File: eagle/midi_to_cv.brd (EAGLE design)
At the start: 100.1 x 82 mm, 35 parts, among them IC2 4504N, IC3 4099N, U1 ATMEGA328P_PDIP

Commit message: starting brd and dac library
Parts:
- removed D1: 1N4148DO35-10, diode:DO35-10
- removed OK1: 6N138, optocoupler:DIL08
- removed PAD1: midi pin 4, wirepad:2,54/0,9
- removed PAD2: midi pin 5, wirepad:2,54/0,9
- removed R2: 220, rcl:0207/10
- removed R3: 270, rcl:0207/10
- added D2: (no value), SparkFun-DiscreteSemi:DIODE-1N4148
- added MIDI_IN: 22-23-2021, con-molex:22-23-2021
- added OK2: 6N138, optocoupler:DIL08
- added R5: 220, rcl:0207/10
- added R6: 270, rcl:0207/10
- added U$11: TLV5628C/I, Texas Instruments_By_element14_Batch_1:DIP16
- moved U$10 300.9 mm to (-69.8, 57.1)
- moved U$9 288.2 mm to (-48.3, 57.1)
- moved U$8 277.1 mm to (-26.7, 57.1)
- moved U$7 256.2 mm to (-69.8, 45.7)
- moved U$6 243.3 mm to (-48.3, 45.7)
- moved R15 228.2 mm to (-57.1, 82.5)
- moved U$2 222.7 mm to (-69.8, 34.3)
- moved U$1 209.5 mm to (-48.3, 34.3)
- moved U$4 204.0 mm to (20.3, 61.0), turned to 270 degrees
- moved C6 203.3 mm to (16.5, 55.9), turned to 180 degrees
- moved C7 199.4 mm to (8.89, 55.9), turned to 180 degrees
- moved U$5 197.9 mm to (5.08, 61.0), turned to 270 degrees
- moved C4 197.1 mm to (16.5, 61.0), turned to 180 degrees
- moved PWR1 195.4 mm to (14.0, 72.4)
- moved C5 192.9 mm to (10.2, 61.0), turned to 180 degrees
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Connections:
- new net N$17: D2.A, MIDI_IN.2, OK2.3
- new net N$18: D2.C, OK2.2, R5.2
- new net N$19: MIDI_IN.1, R5.1
- new net N$20: OK2.6, R6.1
- new net N$21: U$11.15, U$7.13, U$7.14
- new net N$22: U$11.7, U$8.13, U$8.14
- new net N$24: U$11.8, U$9.13, U$9.14
- new net N$28: U$10.13, U$10.14, U$11.9
- new net N$29: U$1.13, U$1.14, U$11.10
- net +12V: now also U$10.10, U$10.9, U$6.10, U$6.9
- net +5V: now also IC3.2, OK2.8, R6.2, U$11.11, U$11.14, U$11.6; no longer OK1.8, R3.2
- net GND: now also OK2.5, U$11.13, U$11.3; no longer OK1.5
- net N$14: now also U$11.5
- net N$15: now also U$11.12
- net N$23: now also U1.4; no longer U1.6
- net N$25: now also U1.6; no longer U1.4
- net N$27: now also U$11.4
- net N$3: now also U$11.2, U$3.13, U$3.14; no longer D1.A, OK1.3, PAD2.1
- net N$30: no longer OK1.6, R3.1
- net N$7: now also U$11.1, U$2.13, U$2.14; no longer D1.C, OK1.2, R2.2
- net N$8: now also U$11.16, U$6.13, U$6.14; no longer PAD1.1, R2.1
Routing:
- net +5V: track 128.9 -> 0.00 mm, vias 2 -> 0
- net GND: track 126.0 -> 0.00 mm
- net N$30: track 31.5 -> 0.00 mm
- net N$1: track 23.0 -> 0.00 mm
- net N$7: track 13.3 -> 0.00 mm
- net N$27: track 12.8 -> 0.00 mm
- net N$4: track 11.7 -> 0.00 mm
- net N$5: track 10.7 -> 0.00 mm
- net N$10: track 10.6 -> 0.00 mm
- net N$3: track 10.5 -> 0.00 mm
- net N$14: track 10.3 -> 0.00 mm
- net N$15: track 8.15 -> 0.00 mm
- net N$8: track 6.13 -> 0.00 mm
- net N$11: track 2.09 -> 0.00 mm
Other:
- board size 100.1 x 82 mm -> 100 x 80 mm

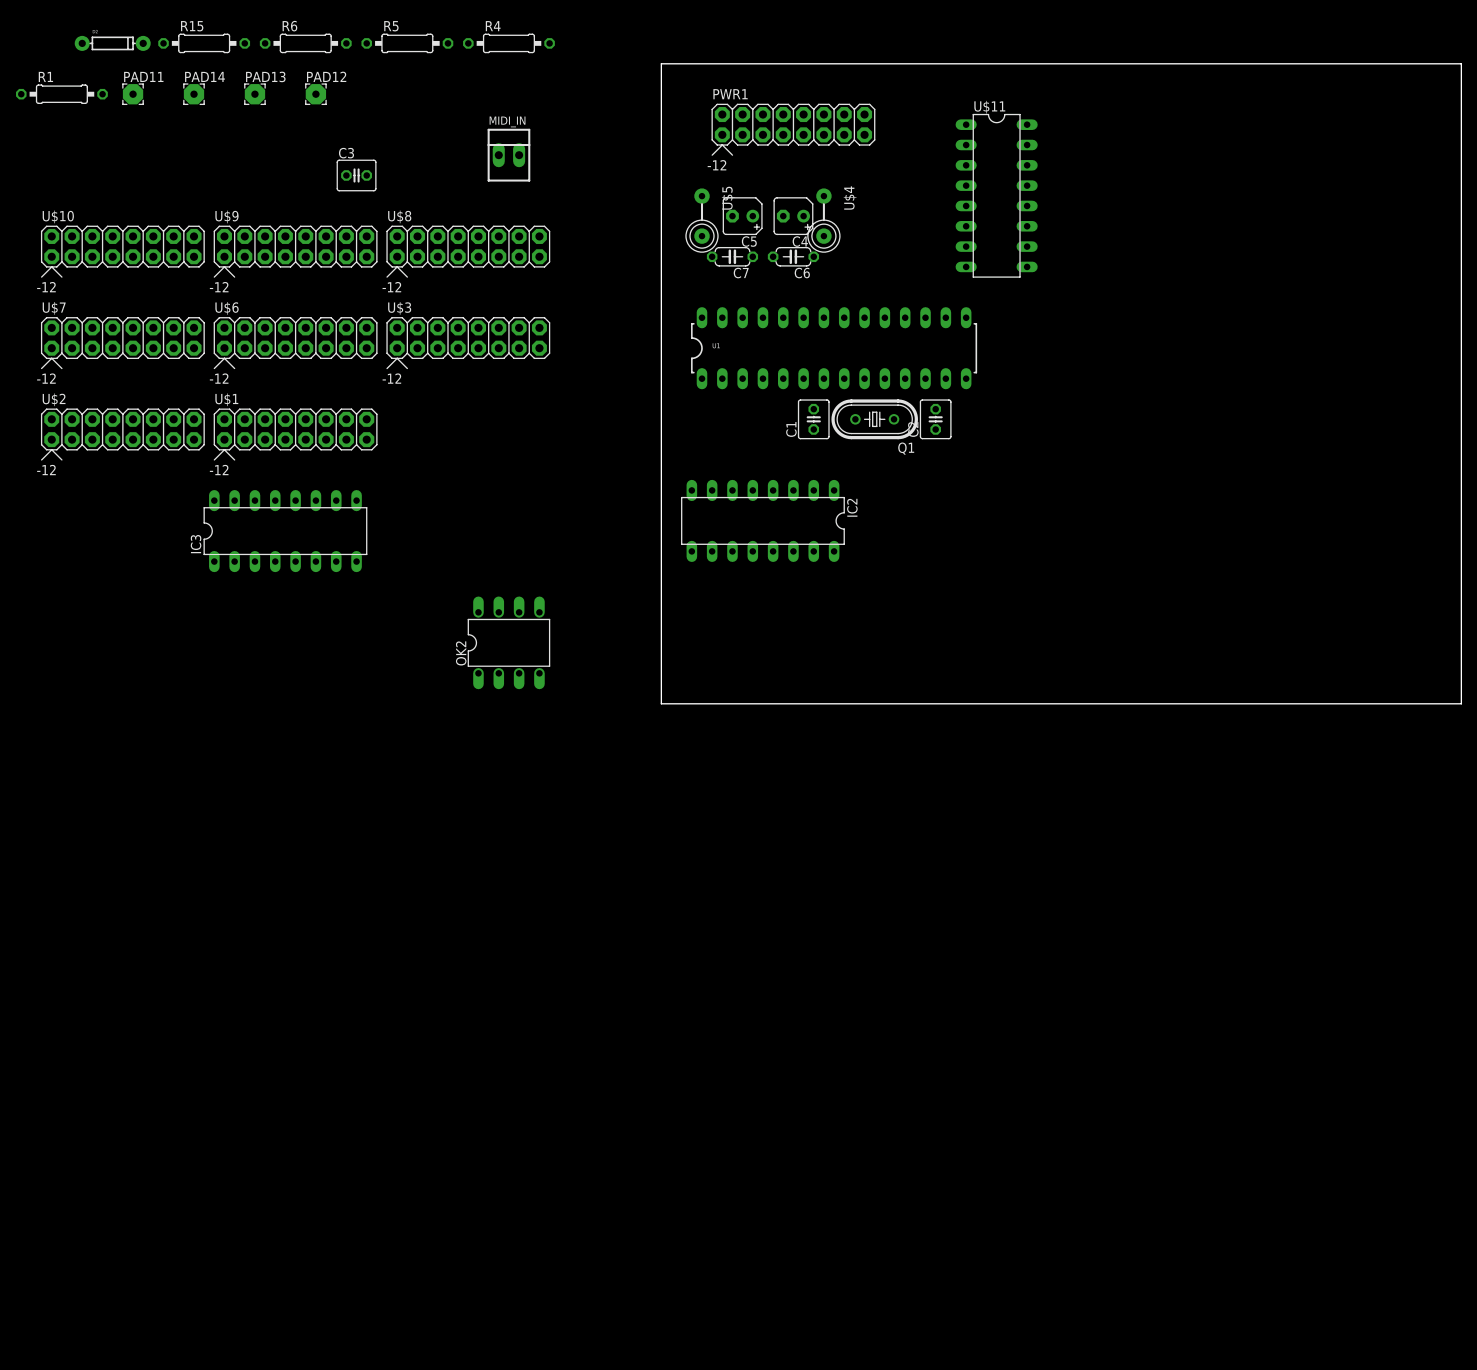
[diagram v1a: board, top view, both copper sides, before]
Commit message: adding output resistors
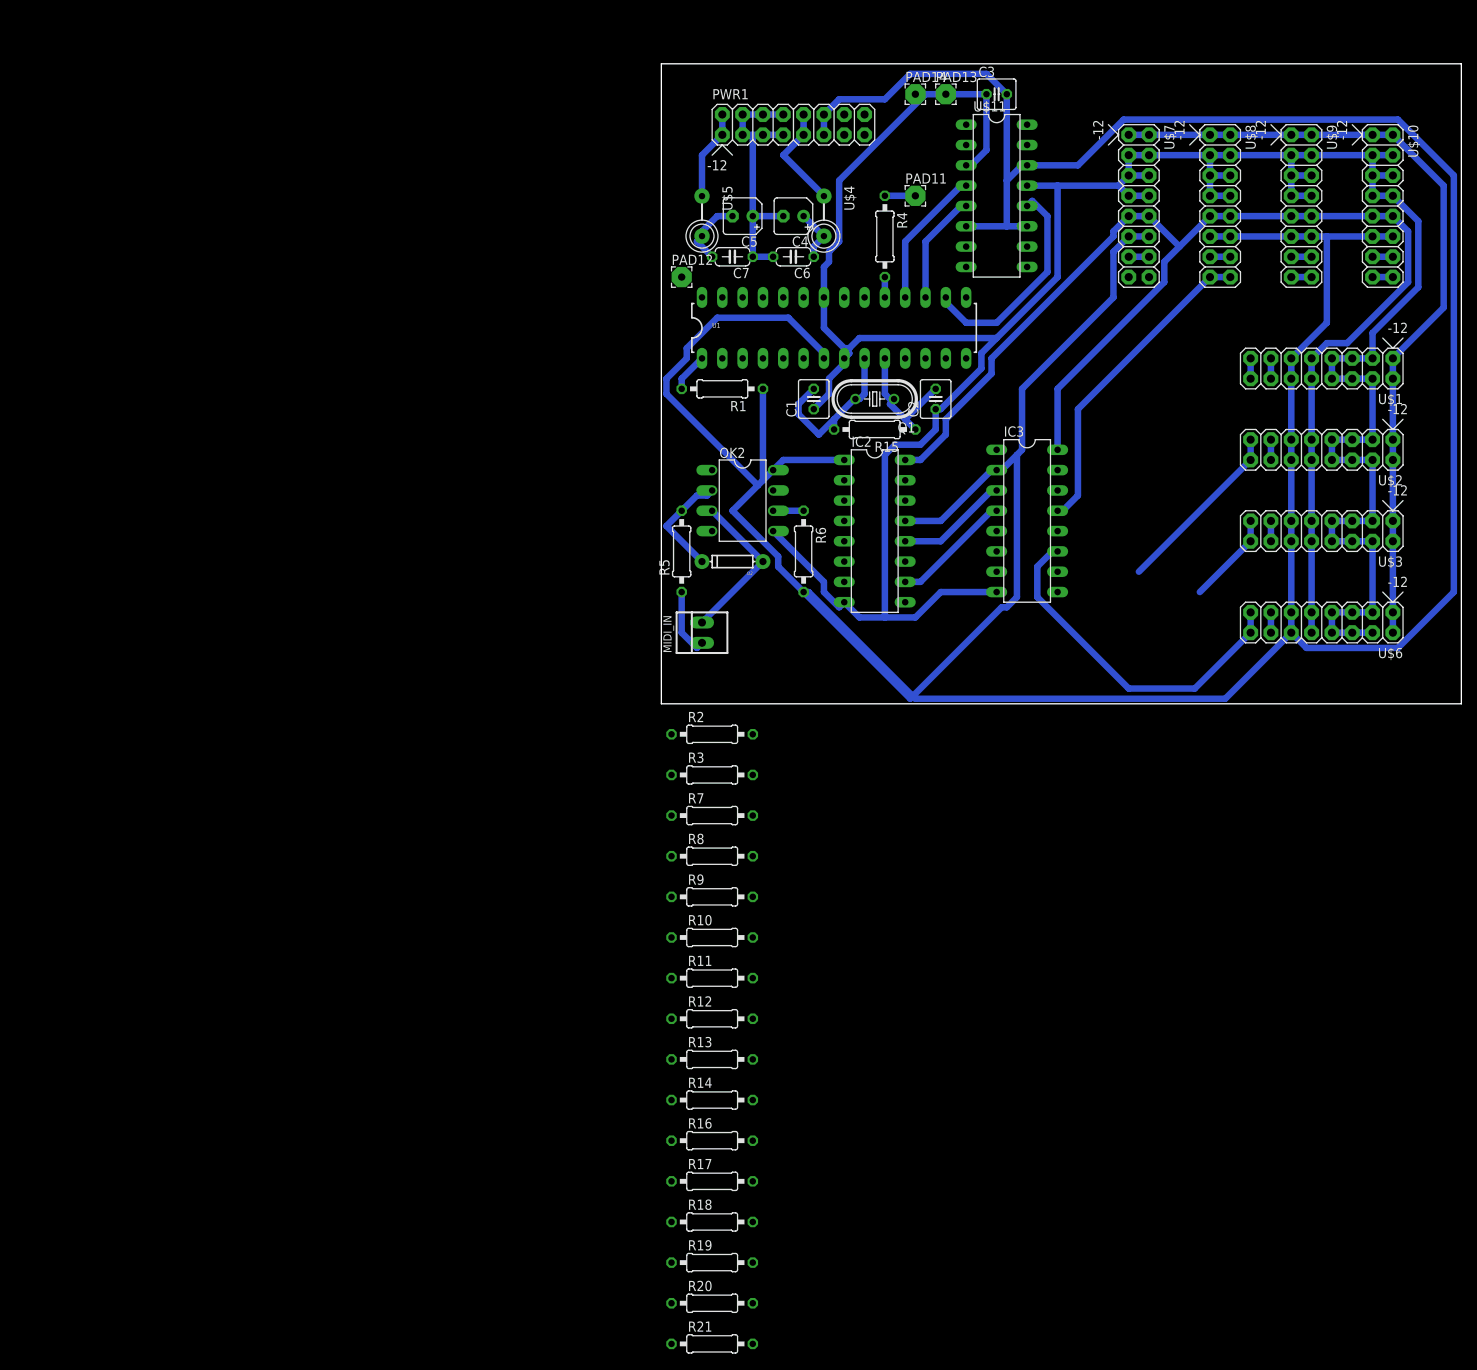
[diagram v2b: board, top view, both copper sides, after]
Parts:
- added R10, R11, R12, R13, R14, R16, R17, R18, R19, R2, R20, R21, R3, R7, R8, R9: 1k, rcl:0207/10
- moved U$10 160.2 mm to (90.2, 64.8), turned to 270 degrees
- moved U$2 155.0 mm to (85.1, 31.8), turned to 180 degrees
- moved U$6 138.0 mm to (85.1, 10.2), turned to 180 degrees
- moved U$1 133.6 mm to (85.1, 41.9), turned to 180 degrees
- moved U$7 130.9 mm to (59.7, 64.8), turned to 270 degrees
- moved U$9 128.5 mm to (80.0, 64.8), turned to 270 degrees
- moved U$3 114.3 mm to (85.1, 21.6), turned to 180 degrees
- moved D2 101.0 mm to (8.89, 17.8), turned to 180 degrees
- moved PAD11 98.6 mm to (31.8, 63.5)
- moved U$8 96.8 mm to (69.8, 64.8), turned to 270 degrees
- moved R15 96.7 mm to (26.7, 34.3), turned to 180 degrees
- moved IC3 92.7 mm to (45.7, 22.9), turned to 270 degrees
- moved R1 90.4 mm to (7.62, 39.4), turned to 180 degrees
- moved PAD14 90.2 mm to (31.8, 76.2)
- moved R6 88.9 mm to (17.8, 19.1), turned to 270 degrees
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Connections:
- new net N$43: IC2.14, U1.28
- new net N$44: IC3.10, R3.1
- new net N$45: IC3.11, R7.1
- new net N$46: IC3.12, R8.1
- new net N$47: IC3.13, R9.1
- new net N$48: IC3.14, R10.1
- new net N$49: IC3.15, R11.1
- new net N$50: IC3.1, R12.1
- new net N$51: R8.2, U$7.15, U$7.16
- new net N$52: R13.1, U$11.2
- new net N$53: R14.1, U$11.1
- new net N$54: R16.1, U$11.16
- new net N$55: R17.1, U$11.15
- new net N$56: R18.1, U$11.7
- new net N$57: R19.1, U$11.8
- new net N$58: R20.1, U$11.9
- new net N$59: R21.1, U$11.10
- net N$12: now also R11.2; no longer IC3.15
- net N$16: now also R12.2; no longer IC3.1
- net N$21: now also R17.2; no longer U$11.15
- net N$22: now also R18.2; no longer U$11.7
- net N$23: now also IC2.3, U1.23; no longer IC2.7, U1.4
- net N$24: now also R19.2; no longer U$11.8
- net N$25: now also IC2.5, U1.24; no longer IC2.3, U1.6
- net N$28: now also R20.2; no longer U$11.9
- net N$29: now also R21.2; no longer U$11.10
- net N$3: now also R13.2; no longer U$11.2
- net N$31: now also IC2.7, U1.25; no longer IC2.5, U1.5
- net N$32: now also IC2.9, U1.26; no longer IC2.11, U1.12
- net N$34: now also IC2.11, U1.27; no longer IC2.9, U1.11
- net N$39: now also IC3.9, R2.1; no longer IC3.12, U$7.15, U$7.16
- net N$40: now also R7.2; no longer IC3.11
- net N$41: now also R3.2; no longer IC3.10
- net N$42: now also R2.2; no longer IC3.9
- net N$6: now also R9.2; no longer IC3.13
- net N$7: now also R14.2; no longer U$11.1
- net N$8: now also R16.2; no longer U$11.16
- net N$9: now also R10.2; no longer IC3.14
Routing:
- net +5V: track 0.00 -> 529.1 mm
- net GND: track 0.00 -> 373.1 mm
- net +12V: track 0.00 -> 177.1 mm
- net -12V: track 0.00 -> 109.3 mm
- net N$40: track 0.00 -> 43.3 mm
- net N$6: track 0.00 -> 39.4 mm
- net N$26: track 0.00 -> 34.3 mm
- net N$15: track 0.00 -> 27.6 mm
- net N$41: track 0.00 -> 22.3 mm
- net N$4: track 0.00 -> 21.1 mm
- net N$17: track 0.00 -> 19.8 mm
- net N$27: track 0.00 -> 17.5 mm
- net N$5: track 0.00 -> 16.8 mm
- net N$37: track 0.00 -> 15.1 mm
- net N$38: track 0.00 -> 14.1 mm
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
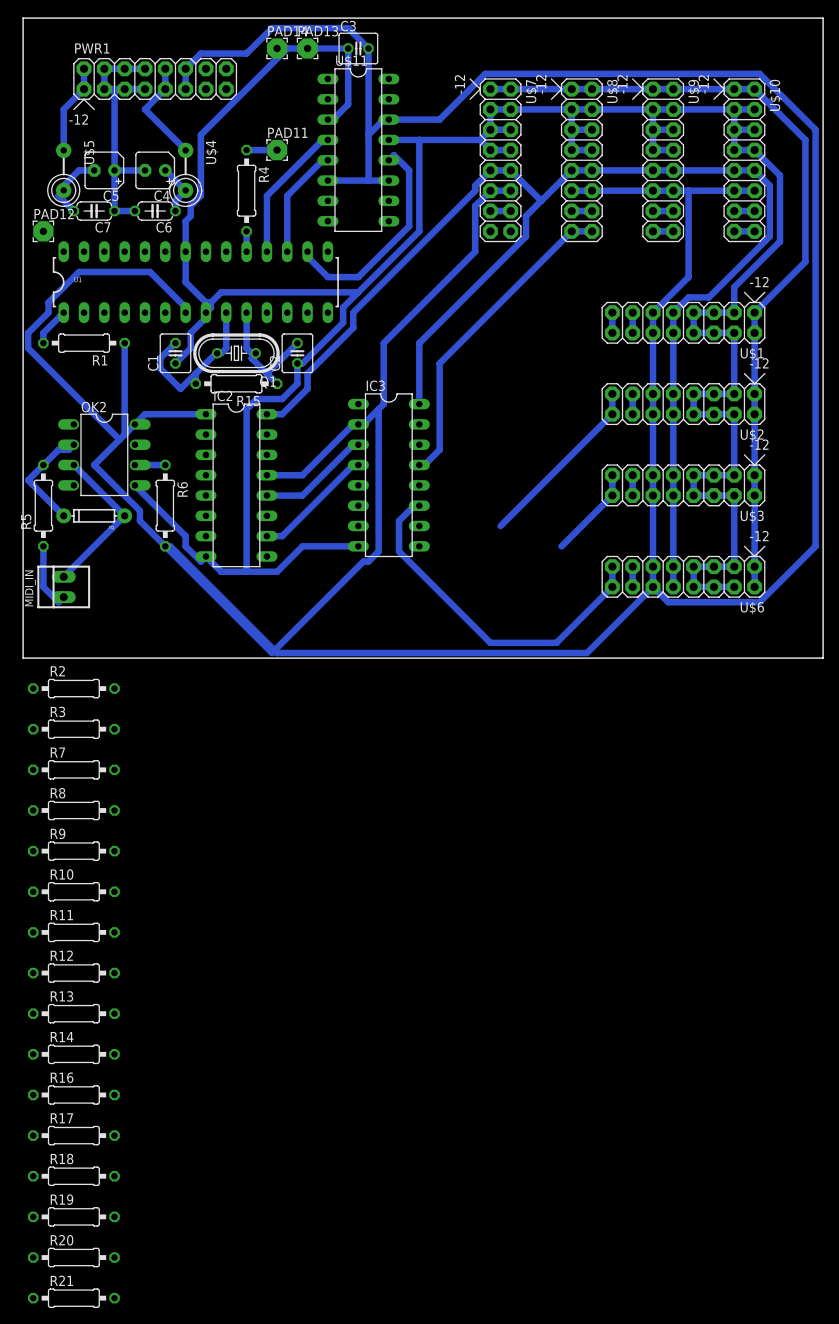
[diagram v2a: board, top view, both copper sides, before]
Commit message: ribbon connectors with interleaved gate cna cv instead of power connectors
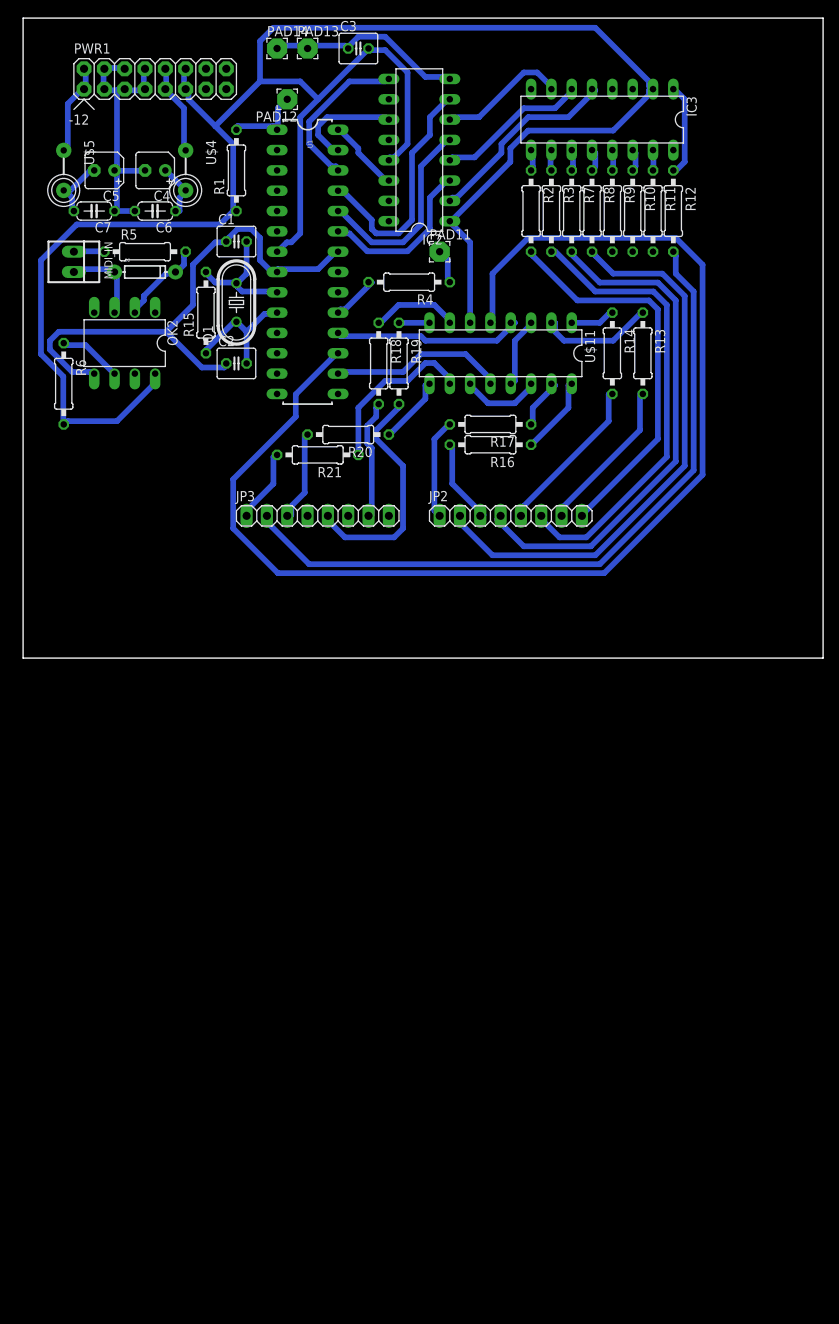
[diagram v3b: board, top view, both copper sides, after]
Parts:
- removed U$1, U$10, U$2, U$3, U$6, U$7, U$8, U$9: POWER, eurorack:POWER_16
- added JP2, JP3: (no value), pinhead:1X08
- moved R12 121.2 mm to (81.3, 55.9), turned to 270 degrees
- moved R11 115.6 mm to (78.7, 55.9), turned to 270 degrees
- moved R19 114.2 mm to (47.0, 36.8), turned to 270 degrees
- moved R14 110.5 mm to (73.7, 38.1), turned to 270 degrees
- moved R10 110.1 mm to (76.2, 55.9), turned to 270 degrees
- moved R21 109.7 mm to (36.8, 25.4), turned to 180 degrees
- moved R13 109.0 mm to (77.5, 38.1), turned to 270 degrees
- moved R18 108.5 mm to (44.5, 36.8), turned to 270 degrees
- moved R20 108.4 mm to (40.6, 27.9), turned to 180 degrees
- moved R9 104.6 mm to (73.7, 55.9), turned to 270 degrees
- moved R17 103.0 mm to (58.4, 29.2), turned to 180 degrees
- moved R8 99.0 mm to (71.1, 55.9), turned to 270 degrees
- moved R16 96.5 mm to (58.4, 26.7), turned to 180 degrees
- moved R7 93.5 mm to (68.6, 55.9), turned to 270 degrees
- moved R3 88.1 mm to (66.0, 55.9), turned to 270 degrees
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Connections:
- net +12V: no longer U$1.10, U$1.9, U$10.10, U$10.9, U$2.10, U$2.9, U$3.10, U$3.9, U$6.10, U$6.9, U$7.10, U$7.9, U$8.10, U$8.9, U$9.10, U$9.9
- net +5V: no longer U$1.11, U$1.12, U$10.11, U$10.12, U$2.11, U$2.12, U$3.11, U$3.12, U$6.11, U$6.12, U$7.11, U$7.12, U$8.11, U$8.12, U$9.11, U$9.12
- net -12V: no longer U$1.1, U$1.2, U$10.1, U$10.2, U$2.1, U$2.2, U$3.1, U$3.2, U$6.1, U$6.2, U$7.1, U$7.2, U$8.1, U$8.2, U$9.1, U$9.2
- net GND: no longer U$1.3, U$1.4, U$1.5, U$1.6, U$1.7, U$1.8, U$10.3, U$10.4, U$10.5, U$10.6, U$10.7, U$10.8, U$2.3, U$2.4, U$2.5, U$2.6, U$2.7, U$2.8, U$3.3, U$3.4, U$3.5, U$3.6, U$3.7, U$3.8, U$6.3, U$6.4, U$6.5, U$6.6, U$6.7, U$6.8, U$7.3, U$7.4, U$7.5, U$7.6, U$7.7, U$7.8, U$8.3, U$8.4, U$8.5, U$8.6, U$8.7, U$8.8, U$9.3, U$9.4, U$9.5, U$9.6, U$9.7, U$9.8
- net N$12: now also JP3.6, R10.2; no longer R11.2, U$10.15, U$10.16
- net N$16: now also JP3.4, R11.2; no longer R12.2, U$1.15, U$1.16
- net N$21: now also JP3.2, R12.2; no longer R17.2, U$7.13, U$7.14
- net N$22: now also JP2.7, R13.2; no longer R18.2, U$8.13, U$8.14
- net N$24: now also JP2.5, R14.2; no longer R19.2, U$9.13, U$9.14
- net N$28: now also JP2.3, R16.2; no longer R20.2, U$10.13, U$10.14
- net N$29: now also JP2.1, R17.2; no longer R21.2, U$1.13, U$1.14
- net N$3: now also JP2.8, R2.2; no longer R13.2, U$3.13, U$3.14
- net N$40: now also JP3.7, R18.2; no longer R7.2, U$6.15, U$6.16
- net N$41: now also JP3.5, R19.2; no longer R3.2, U$2.15, U$2.16
- net N$42: now also JP3.3, R20.2; no longer R2.2, U$3.15, U$3.16
- net N$51: now also JP3.1, R21.2; no longer R8.2, U$7.15, U$7.16
- net N$6: now also JP2.6, R3.2; no longer R9.2, U$8.15, U$8.16
- net N$7: now also JP2.4, R7.2; no longer R14.2, U$2.13, U$2.14
- net N$8: now also JP2.2, R8.2; no longer R16.2, U$6.13, U$6.14
- net N$9: now also JP3.8, R9.2; no longer R10.2, U$9.15, U$9.16
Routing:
- net GND: track 373.1 -> 101.8 mm
- net +5V: track 529.1 -> 264.4 mm
- net +12V: track 177.1 -> 6.94 mm
- net N$14: track 13.9 -> 155.6 mm
- net -12V: track 109.3 -> 7.75 mm
- net N$21: track 2.54 -> 89.7 mm
- net N$8: track 2.54 -> 70.7 mm
- net N$7: track 2.54 -> 64.6 mm
- net N$3: track 2.54 -> 48.7 mm
- net N$31: track 0.00 -> 30.0 mm
- net N$40: track 43.3 -> 15.1 mm
- net N$25: track 0.00 -> 25.2 mm
- net N$33: track 0.00 -> 25.0 mm
- net N$59: track 0.00 -> 21.3 mm
- net N$23: track 0.00 -> 21.0 mm
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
